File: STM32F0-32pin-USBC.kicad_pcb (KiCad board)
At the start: 2 copper layers, 0 parts

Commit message: finished part nubers in BOM
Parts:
- added C1: 10u, Capacitor_SMD:C_1206_3216Metric_Pad1.33x1.80mm_HandSolder, F.Cu at (111.3, 107.2)
- added C2: 1u, Capacitor_SMD:C_1206_3216Metric_Pad1.33x1.80mm_HandSolder, F.Cu at (111.3, 110.5)
- added C3: 1u, Capacitor_SMD:C_1206_3216Metric_Pad1.33x1.80mm_HandSolder, F.Cu at (111.3, 113.9)
- added C4: 100n, Capacitor_SMD:C_1206_3216Metric_Pad1.33x1.80mm_HandSolder, F.Cu at (116.3, 51.5)
- added C5: 100n, Capacitor_SMD:C_1206_3216Metric_Pad1.33x1.80mm_HandSolder, F.Cu at (116.3, 54.9)
- added C6: 100n, Capacitor_SMD:C_1206_3216Metric_Pad1.33x1.80mm_HandSolder, F.Cu at (116.3, 58.2)
- added C7: 100n, Capacitor_SMD:C_1206_3216Metric_Pad1.33x1.80mm_HandSolder, F.Cu at (116.3, 61.6)
- added D1: LED, LED_SMD:LED_1206_3216Metric_Pad1.42x1.75mm_HandSolder, F.Cu at (110.4, 51.5)
- added D2: LED, LED_SMD:LED_1206_3216Metric_Pad1.42x1.75mm_HandSolder, F.Cu at (110.4, 54.9)
- added D3: LED, LED_SMD:LED_1206_3216Metric_Pad1.42x1.75mm_HandSolder, F.Cu at (110.4, 58.3)
- added D4: LED, LED_SMD:LED_1206_3216Metric_Pad1.42x1.75mm_HandSolder, F.Cu at (110.4, 61.7)
- added H1: M3, MountingHole:MountingHole_3.2mm_M3, F.Cu at (237.7, 80.8)
- added H2: M3, MountingHole:MountingHole_3.2mm_M3, F.Cu at (237.7, 88.7)
- added H3: M3, MountingHole:MountingHole_3.2mm_M3, F.Cu at (237.7, 96.7)
- added H4: M3, MountingHole:MountingHole_3.2mm_M3, F.Cu at (237.7, 104.6)
- added J1: Conn_ARM_JTAG_SWD_10, Connector_PinHeader_1.27mm:PinHeader_2x05_P1.27mm_Vertical, F.Cu at (117.6, 90.4)
- added J2: USB_C_Receptacle_USB2.0_16P, Connector_USB:USB_C_Receptacle_GCT_USB4085, F.Cu at (86.7, 80.9)
- added J3: Conn_01x12, Connector_PinHeader_2.54mm:PinHeader_1x12_P2.54mm_Vertical, F.Cu at (133.1, 70.6)
- added JP1: Jumper_2_Bridged, Jumper:SolderJumper-2_P1.3mm_Bridged_RoundedPad1.0x1.5mm, F.Cu at (93.9, 73.0)
- added R1: 5K1, Resistor_SMD:R_1206_3216Metric_Pad1.30x1.75mm_HandSolder, F.Cu at (117.3, 107.2)
- added R2: 5K1, Resistor_SMD:R_1206_3216Metric_Pad1.30x1.75mm_HandSolder, F.Cu at (117.3, 110.4)
- added R3: ??, Resistor_SMD:R_1206_3216Metric_Pad1.30x1.75mm_HandSolder, F.Cu at (117.3, 113.7)
- added R4: 270R, Resistor_SMD:R_1206_3216Metric_Pad1.30x1.75mm_HandSolder, F.Cu at (122.3, 51.5)
- added R5: 270R, Resistor_SMD:R_1206_3216Metric_Pad1.30x1.75mm_HandSolder, F.Cu at (122.3, 54.8)
- added R6: 270R, Resistor_SMD:R_1206_3216Metric_Pad1.30x1.75mm_HandSolder, F.Cu at (122.3, 58.1)
- added R7: 270R, Resistor_SMD:R_1206_3216Metric_Pad1.30x1.75mm_HandSolder, F.Cu at (122.3, 61.4)
- added TP1: TestPoint_2Pole, TestPoint:TestPoint_2Pads_Pitch2.54mm_Drill0.8mm, F.Cu at (88.4, 66.2)
- added TP2: TestPoint_2Pole, TestPoint:TestPoint_2Pads_Pitch2.54mm_Drill0.8mm, F.Cu at (88.4, 69.6)
- added U1: STM32F042K6Tx, Package_QFP:LQFP-32_7x7mm_P0.8mm, F.Cu at (118.0, 78.3)
- added U2: USBLC6-2SC6, Package_TO_SOT_SMD:SOT-23-6, F.Cu at (93.1, 84.3)
- added U3: MCP1755S, Package_TO_SOT_SMD:SOT-223-3_TabPin2, F.Cu at (103.1, 79.2)
- added U4: MCP2221AxSL, Package_SO:SOIC-14_3.9x8.7mm_P1.27mm, F.Cu at (98.0, 93.5)

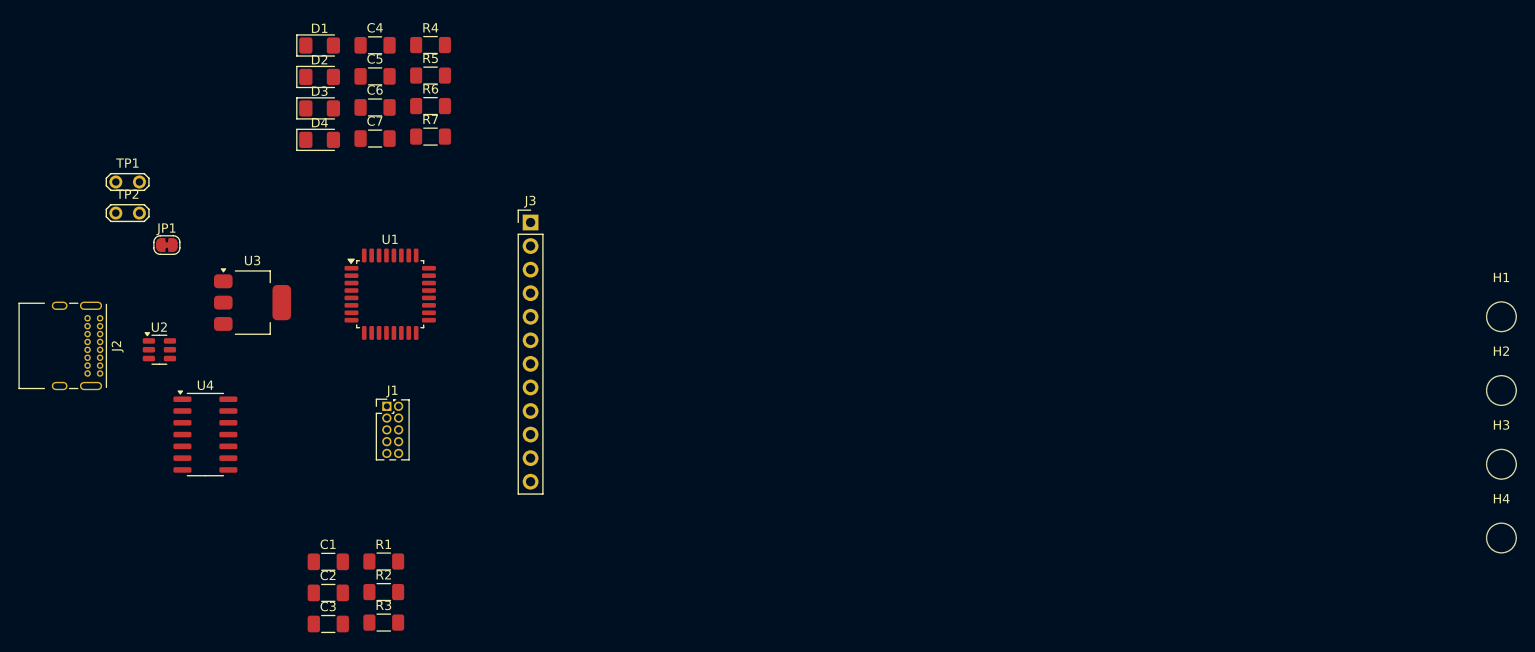
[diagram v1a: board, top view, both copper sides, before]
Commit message: preliminary footprint placement
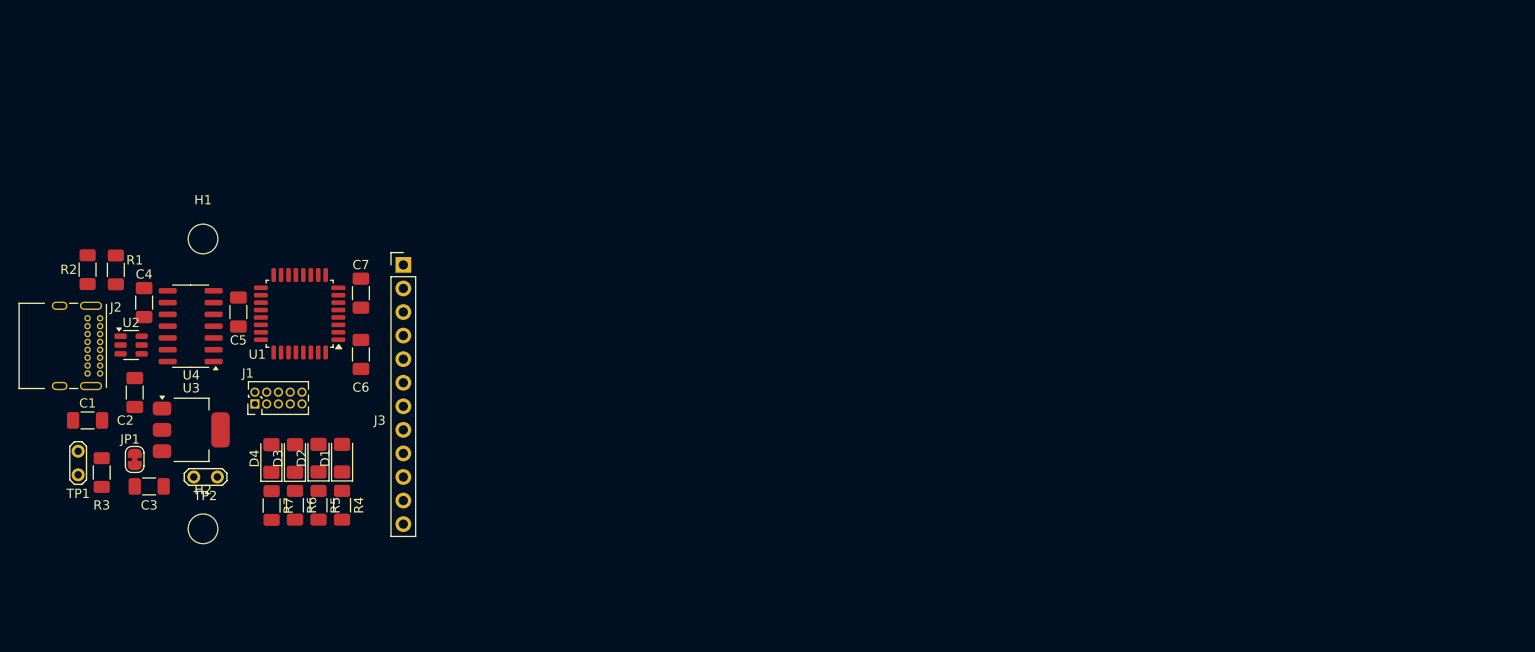
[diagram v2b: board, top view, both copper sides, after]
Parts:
- removed H3, H4: M3, MountingHole:MountingHole_3.2mm_M3
- moved H2 140.7 mm to (97.8, 103.6)
- moved H1 140.2 mm to (97.8, 72.4)
- moved R4 50.5 mm to (112.8, 101.1), turned to -90 degrees
- moved R5 47.9 mm to (110.2, 101.1), turned to -90 degrees
- moved R2 47.2 mm to (85.3, 75.7), turned to 90 degrees
- moved R6 45.4 mm to (107.7, 101.1), turned to -90 degrees
- moved D1 44.5 mm to (112.8, 96.0), turned to 90 degrees
- moved R7 43.3 mm to (105.2, 101.1), turned to -90 degrees
- moved R1 42.7 mm to (88.4, 75.7), turned to 90 degrees
- moved D2 41.1 mm to (110.2, 96.0), turned to 90 degrees
- moved D3 37.8 mm to (107.7, 96.0), turned to 90 degrees
- moved C4 37.3 mm to (91.4, 79.2), turned to 90 degrees
- moved D4 34.7 mm to (105.2, 96.0), turned to 90 degrees
- moved R3 34.4 mm to (86.9, 97.6), turned to -90 degrees
- moved C1 30.1 mm to (85.3, 91.9)
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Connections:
- net Net-(J2-D+-PadA6) renamed /USB_and_LDO/D+_conn
- net Net-(J2-D--PadA7) renamed /USB_and_LDO/D-_conn

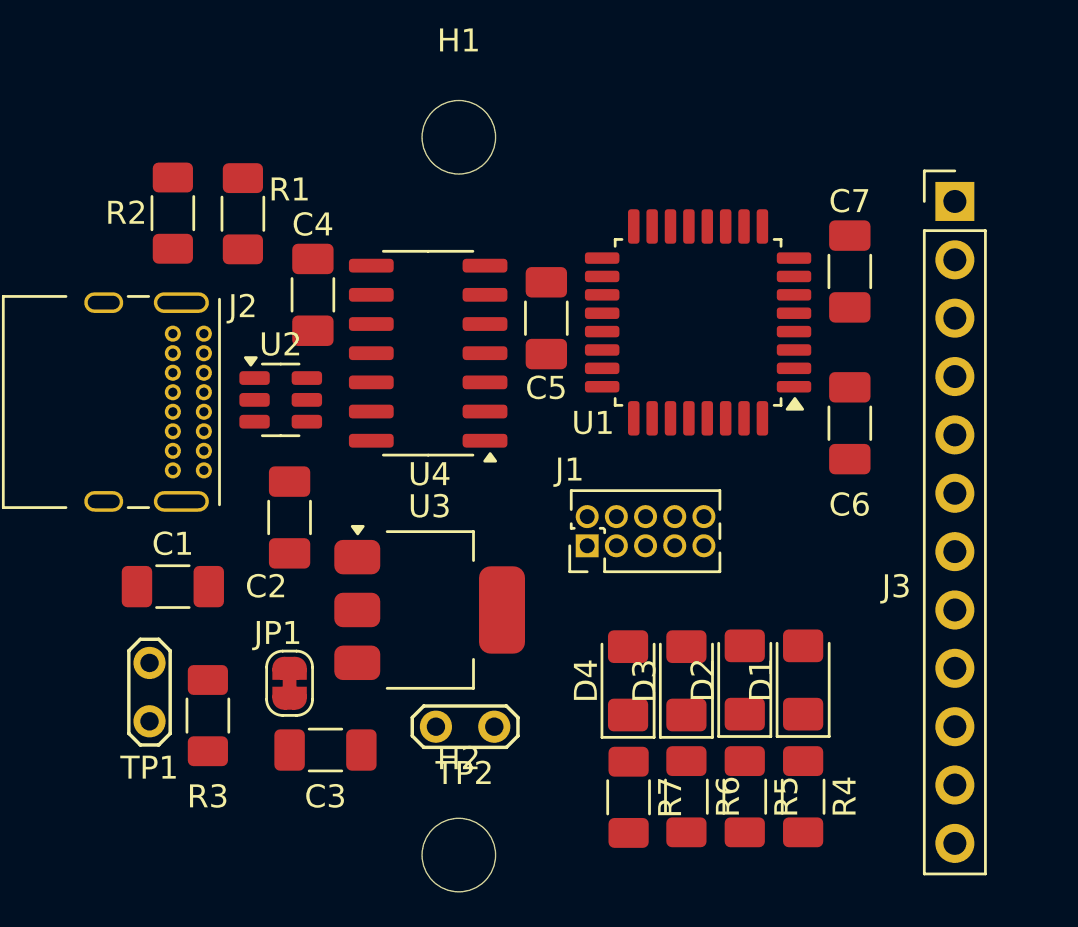
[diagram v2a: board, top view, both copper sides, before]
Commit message: everything routed but ground
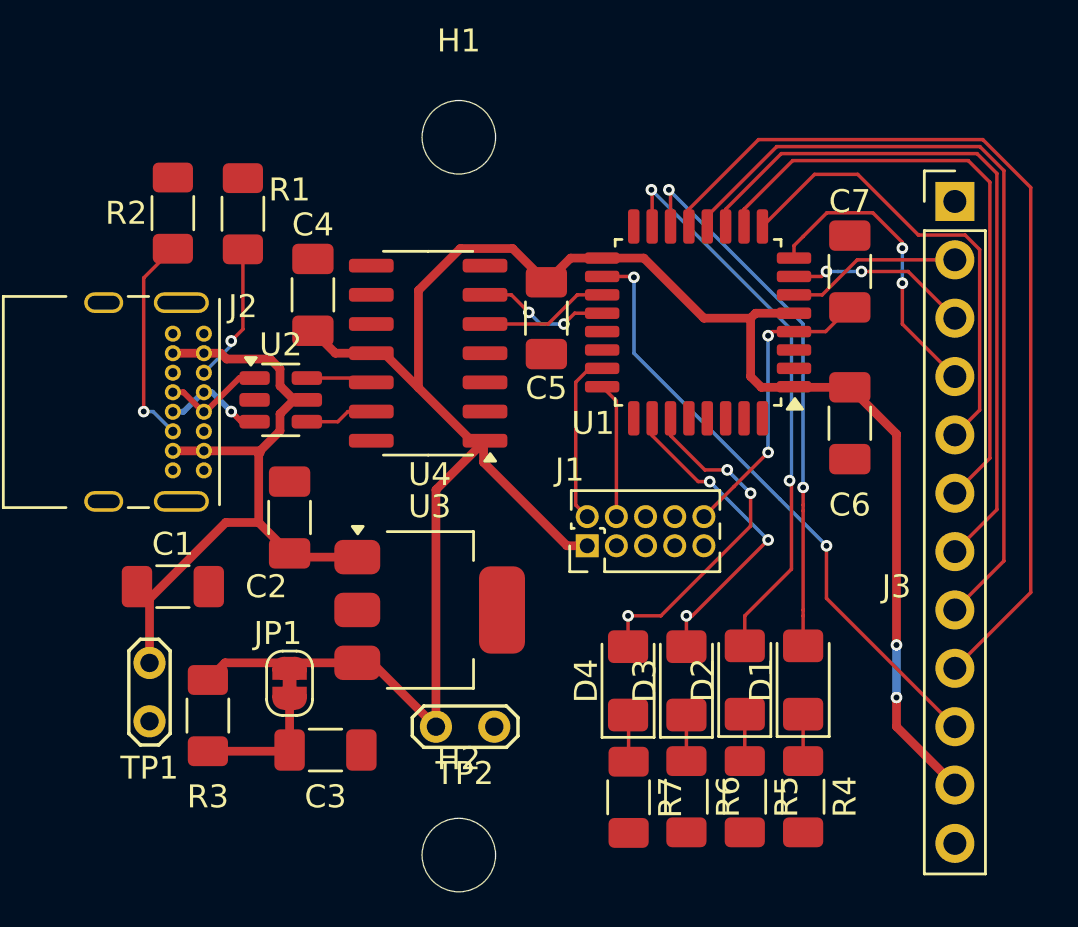
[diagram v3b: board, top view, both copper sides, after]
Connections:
- net Net-(JP1-A) renamed /USB_and_LDO/ldo_jumper
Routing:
- net +3.3V: track 0.00 -> 91.0 mm, vias 0 -> 2
- net /PA7: track 0.00 -> 40.0 mm
- net /PA6: track 0.00 -> 35.1 mm
- net /PA5: track 0.00 -> 31.1 mm
- net VBUS: track 0.00 -> 30.7 mm
- net /PA4: track 0.00 -> 26.9 mm
- net /PA8: track 0.00 -> 26.7 mm, vias 0 -> 2
- net /PB1: track 0.00 -> 24.9 mm, vias 0 -> 2
- net /PB0: track 0.00 -> 23.9 mm, vias 0 -> 2
- net /PA3: track 0.00 -> 20.3 mm
- net /PB4: track 0.00 -> 15.0 mm, vias 0 -> 3
- net /PB3: track 0.00 -> 13.9 mm, vias 0 -> 3
- net /PA2: track 0.00 -> 13.2 mm, vias 0 -> 2
- net /NRESET: track 0.00 -> 13.1 mm, vias 0 -> 2
- net /USB_and_LDO/CC2: track 0.00 -> 9.24 mm, vias 0 -> 1
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
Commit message: routing done; many ERC violations
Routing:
- net GND: track 0.00 -> 51.1 mm, vias 0 -> 24
- net /PB1: track 24.9 -> 61.7 mm, vias 2 -> 0
- net /PB0: track 23.9 -> 54.4 mm, vias 2 -> 0
- net /PA8: track 26.7 -> 54.8 mm, vias 2 -> 3
- net /NRESET: track 13.1 -> 22.4 mm
- net /PB4: track 15.0 -> 17.6 mm, vias 3 -> 2
- net /PB3: track 13.9 -> 14.7 mm, vias 3 -> 2
- added copper zone on B.Cu, net GND

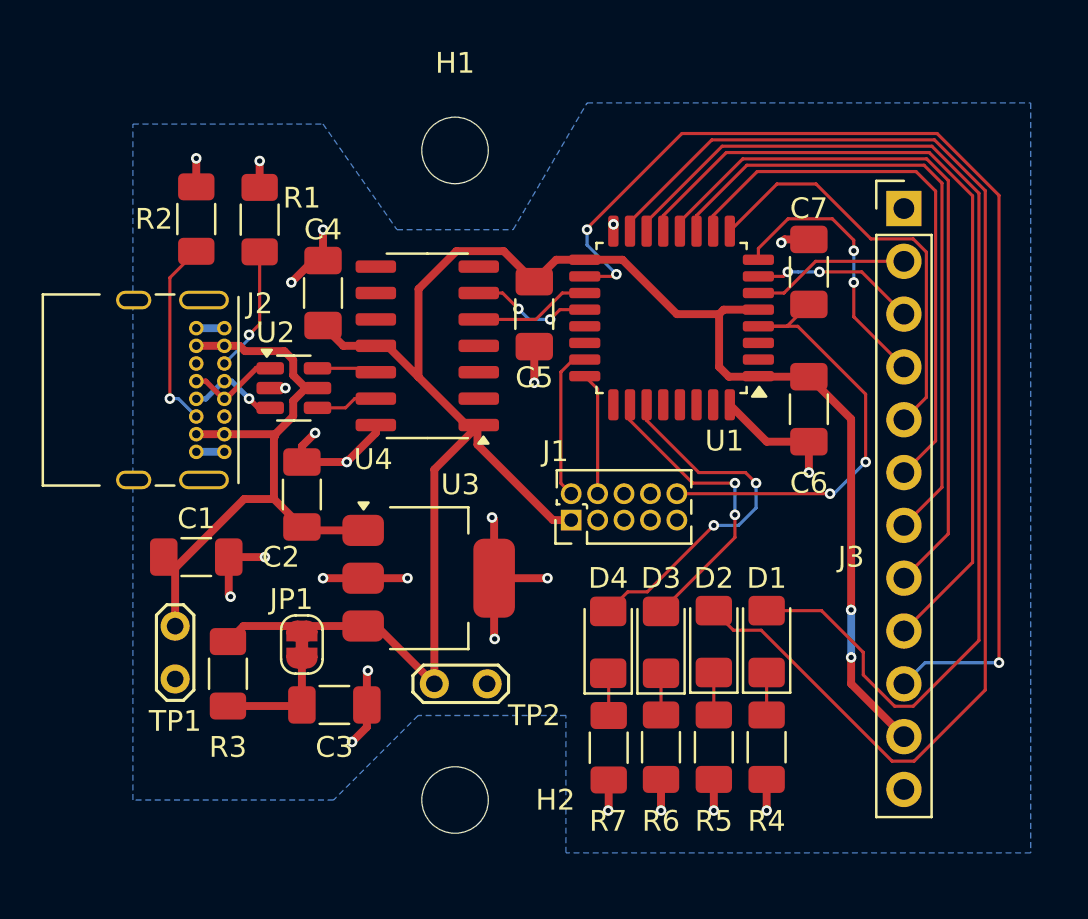
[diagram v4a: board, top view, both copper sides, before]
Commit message: switched to small pad size usb conn and drew board edge
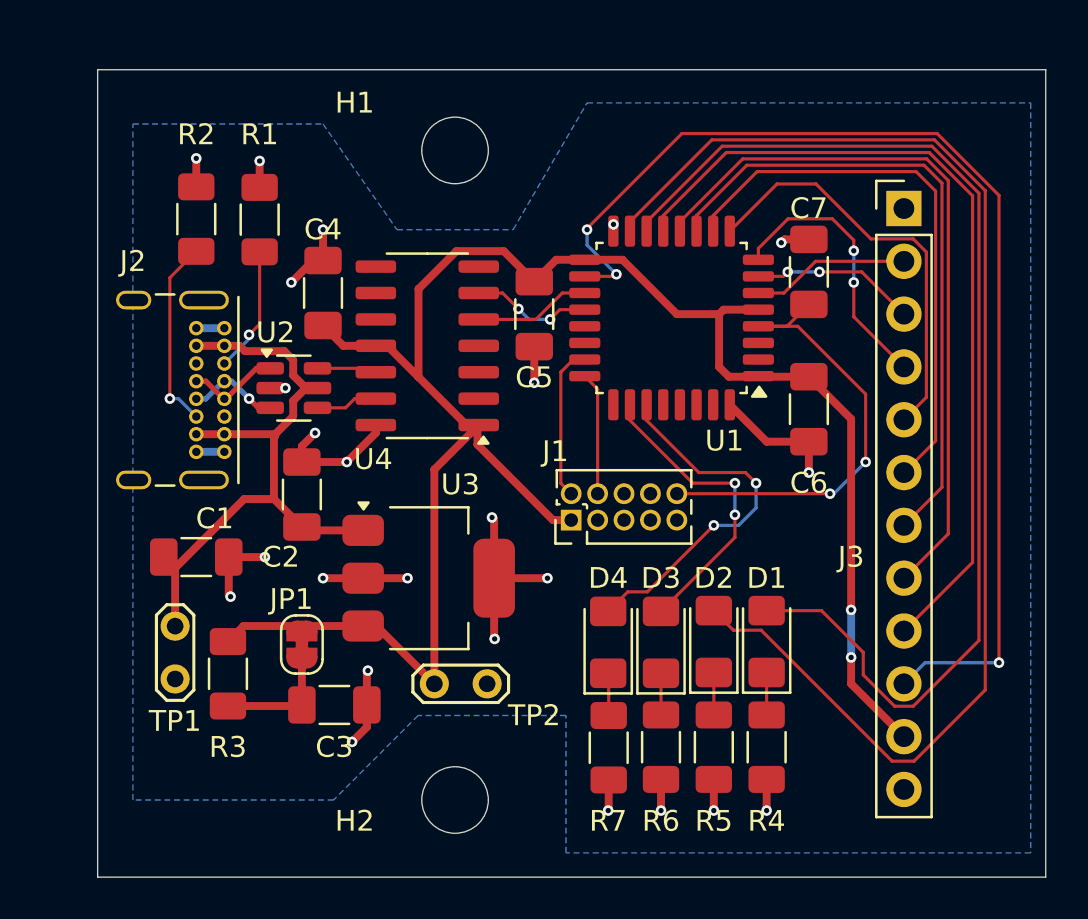
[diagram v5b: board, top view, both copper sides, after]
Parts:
- J2: footprint Connector_USB:USB_C_Receptacle_GCT_USB4085 -> AAAA_HugonLib:USB_C_Receptacle_GCT_USB4085_Reduced_Pad_Size
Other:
- board outline added: 45.6 x 38.8 mm
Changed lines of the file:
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@@
 		(tags "capacitor handsolder")
 		(property "Reference" "C1"
-			(at 0 -1.85 0)
+			(at 0.889 -1.85 0)
 			(layer "F.SilkS")
 			(effects
@@
 		(tags "resistor handsolder")
 		(property "Reference" "R1"
-			(at 1.042 2.032 180)
+			(at 4.09 0 180)
 			(layer "F.SilkS")
 			(effects
@@
 		(tags "mounting hole 3.2mm no annular m3")
 		(property "Reference" "H1"
-			(at 0 -4.2 0)
+			(at -4.826 -2.286 0)
 			(layer "F.SilkS")
 			(effects
@@
 		(tags "resistor handsolder")
 		(property "Reference" "R2"
-			(at 0 -2.032 0)
+			(at 4.064 0 0)
 			(layer "F.SilkS")
 			(effects
@@
 		)
 	)
-	(footprint "Connector_USB:USB_C_Receptacle_GCT_USB4085"
+	(footprint "AAAA_HugonLib:USB_C_Receptacle_GCT_USB4085_Reduced_Pad_Size"
 		(layer "F.Cu")
 		(at 86.694 80.938 -90)
@@
 		(tags "USB Type-C Receptacle Through-hole Right angle")
 		(property "Reference" "J2"
-			(at -1.182 -1.698 180)
+			(at -3.214 4.398 0)
 			(layer "F.SilkS")
 			(effects
@@
 		)
 		(property "Value" "USB_C_Receptacle_USB2.0_16P"
-			(at 2.975 9.925 90)
+			(at 2.975 9.925 -90)
 			(layer "F.Fab")
 			(effects
@@
 			)
 		)
-		(property "Footprint" "Connector_USB:USB_C_Receptacle_GCT_USB4085"
+		(property "Footprint" "AAAA_HugonLib:USB_C_Receptacle_GCT_USB4085_Reduced_Pad_Size"
 			(at 0 0 -90)
 			(unlocked yes)
@@
 		(attr through_hole)
 		(fp_line
-			(start -1.62 8.73)
-			(end 7.57 8.73)
-			(stroke
-				(width 0.12)
-				(type solid)
-			)
-			(layer "F.SilkS")
-		)
-		(fp_line
-			(start -1.62 6)
-			(end -1.62 8.73)
-			(stroke
-				(width 0.12)
-				(type solid)
-			)
-			(layer "F.SilkS")
-		)
-		(fp_line
-			(start 7.57 6)
-			(end 7.57 8.73)
-			(stroke
-				(width 0.12)
-				(type solid)
-			)
-			(layer "F.SilkS")
-		)
-		(fp_line
 			(start -1.62 2.4)
 			(end -1.62 3.3)
@@
 		)
 		(fp_text user "PCB Edge"
-			(at 2.975 6.1 90)
+			(at 2.975 6.1 -90)
 			(layer "Dwgs.User")
 			(effects
@@
 		)
 		(fp_text user "${REFERENCE}"
-			(at 2.975 4.025 90)
+			(at 2.975 4.025 -90)
 			(layer "F.Fab")
 			(effects
@@
 		(pad "A1" thru_hole circle
 			(at 0 0 270)
-			(size 0.7 0.7)
+			(size 0.69746 0.69746)
 			(drill 0.4)
 			(layers "*.Cu" "*.Mask")
@@
 		(pad "A4" thru_hole circle
 			(at 0.85 0 270)
-			(size 0.7 0.7)
+			(size 0.69746 0.69746)
 			(drill 0.4)
 			(layers "*.Cu" "*.Mask")
@@
 		(pad "A5" thru_hole circle
 			(at 1.7 0 270)
-			(size 0.7 0.7)
+			(size 0.69746 0.69746)
 			(drill 0.4)
 			(layers "*.Cu" "*.Mask")
@@
 		(pad "A6" thru_hole circle
 			(at 2.55 0 270)
-			(size 0.7 0.7)
+			(size 0.69746 0.69746)
 			(drill 0.4)
 			(layers "*.Cu" "*.Mask")
@@
 		(pad "A7" thru_hole circle
 			(at 3.4 0 270)
-			(size 0.7 0.7)
+			(size 0.69746 0.69746)
 			(drill 0.4)
 			(layers "*.Cu" "*.Mask")
@@
 		(pad "A8" thru_hole circle
 			(at 4.25 0 270)
-			(size 0.7 0.7)
+			(size 0.69746 0.69746)
 			(drill 0.4)
 			(layers "*.Cu" "*.Mask")
@@
 		(pad "A9" thru_hole circle
 			(at 5.1 0 270)
-			(size 0.7 0.7)
+			(size 0.69746 0.69746)
 			(drill 0.4)
 			(layers "*.Cu" "*.Mask")
@@
 		(pad "A12" thru_hole circle
 			(at 5.95 0 270)
-			(size 0.7 0.7)
+			(size 0.69746 0.69746)
 			(drill 0.4)
 			(layers "*.Cu" "*.Mask")
@@
 		(pad "B1" thru_hole circle
 			(at 5.95 1.35 270)
-			(size 0.7 0.7)
+			(size 0.69746 0.69746)
 			(drill 0.4)
 			(layers "*.Cu" "*.Mask")
@@
 		(pad "B4" thru_hole circle
 			(at 5.1 1.35 270)
-			(size 0.7 0.7)
+			(size 0.69746 0.69746)
 			(drill 0.4)
 			(layers "*.Cu" "*.Mask")
@@
 		(pad "B5" thru_hole circle
 			(at 4.25 1.35 270)
-			(size 0.7 0.7)
+			(size 0.69746 0.69746)
 			(drill 0.4)
 			(layers "*.Cu" "*.Mask")
@@
 		(pad "B6" thru_hole circle
 			(at 3.4 1.35 270)
-			(size 0.7 0.7)
+			(size 0.69746 0.69746)
 			(drill 0.4)
 			(layers "*.Cu" "*.Mask")
@@
 		(pad "B7" thru_hole circle
 			(at 2.55 1.35 270)
-			(size 0.7 0.7)
+			(size 0.69746 0.69746)
 			(drill 0.4)
 			(layers "*.Cu" "*.Mask")
@@
 		(pad "B8" thru_hole circle
 			(at 1.7 1.35 270)
-			(size 0.7 0.7)
+			(size 0.69746 0.69746)
 			(drill 0.4)
 			(layers "*.Cu" "*.Mask")
@@
 		(pad "B9" thru_hole circle
 			(at 0.85 1.35 270)
-			(size 0.7 0.7)
+			(size 0.69746 0.69746)
 			(drill 0.4)
 			(layers "*.Cu" "*.Mask")
@@
 		(pad "B12" thru_hole circle
 			(at 0 1.35 270)
-			(size 0.7 0.7)
+			(size 0.69746 0.69746)
 			(drill 0.4)
 			(layers "*.Cu" "*.Mask")
@@
 		(tags "mounting hole 3.2mm no annular m3")
 		(property "Reference" "H2"
-			(at 4.826 0 0)
+			(at -4.826 1.016 0)
 			(layer "F.SilkS")
 			(effects
@@
 		)
 	)
+	(gr_rect
+		(start 80.6 68.508)
+		(end 126.2 107.342)
+		(stroke
+			(width 0.05)
+			(type default)
+		)
+		(fill none)
+		(layer "Edge.Cuts")
+	)
 	(segment
